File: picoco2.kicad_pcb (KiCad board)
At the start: 2 copper layers, 54.5 x 103.4 mm, 41 parts, among them J1 Conn_01x03_Female, J2 Micro_SD_Card, J3 Conn_01x03_Female, Q1 Q_NMOS_GDS, SW1 SW_Push, SW2 SW_Push, U1 PicoW, U2 scd30, U3 ssd1306, U4 PCF8523T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

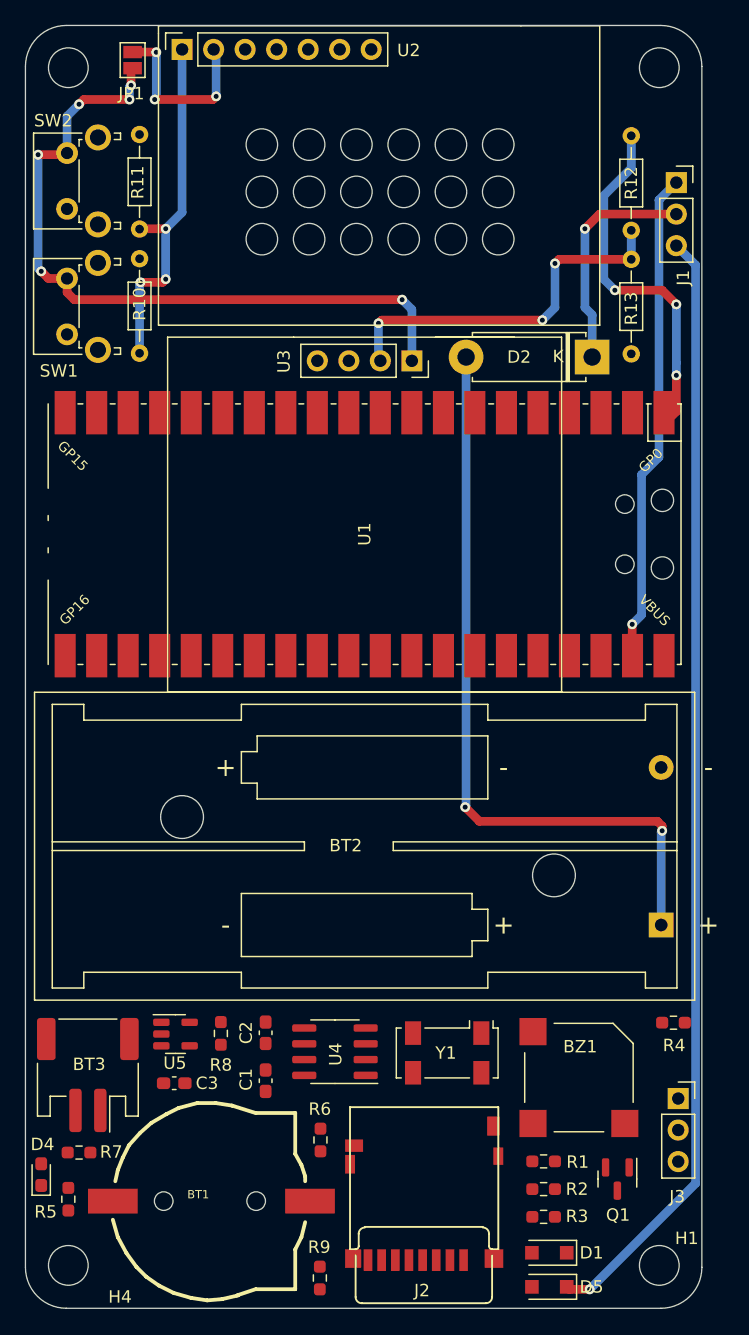
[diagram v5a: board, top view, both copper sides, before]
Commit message: finished positioning of holes and parts
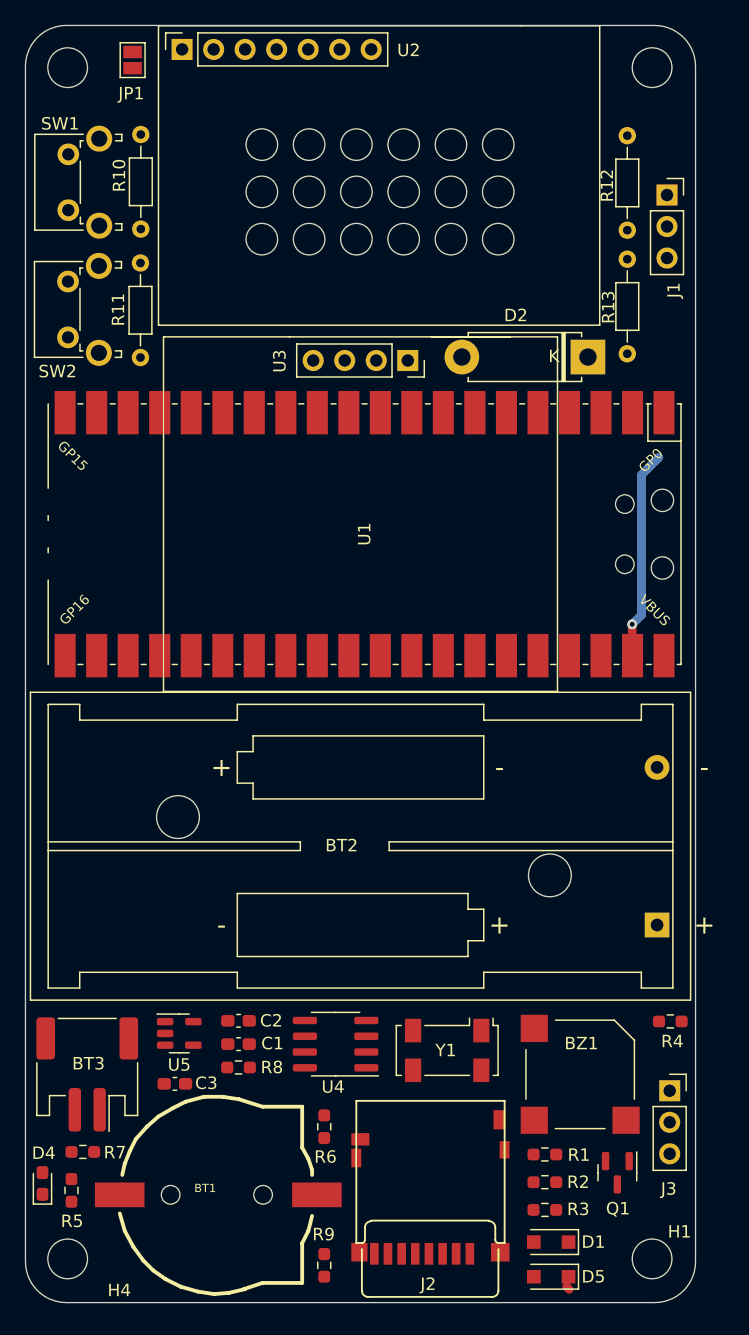
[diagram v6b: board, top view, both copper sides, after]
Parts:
- moved SW2 10.4 mm to (3.43, 25.1)
- moved R11 10.4 mm to (9.27, 26.8)
- moved R10 10.0 mm to (9.30, 16.4)
- moved SW1 10.0 mm to (3.45, 14.9)
- moved C1 3.67 mm to (17.2, 82.1), turned to 180 degrees
- moved R8 3.09 mm to (17.2, 84.0), turned to 0 degrees
- moved C2 2.39 mm to (17.2, 80.2), turned to 180 degrees
- moved J1 1.25 mm to (51.7, 13.7)
- moved R6 1.11 mm to (24.1, 88.7)
- moved R9 1.08 mm to (24.1, 99.9)
- moved J3 0.93 mm to (51.9, 85.9)
- moved D1 0.88 mm to (42.4, 98.0)
- moved D5 0.83 mm to (42.4, 100.8)
- moved H1 0.78 mm to (50.5, 99.4)
- moved R5 0.76 mm to (3.71, 93.9)
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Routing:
- net Net-(D5-Pad1): track 90.2 -> 0.29 mm, vias 1 -> 0
- net VBAT_AAA: track 60.8 -> 0.00 mm, vias 2 -> 0
- net +3V3: track 59.1 -> 0.22 mm, vias 6 -> 0
- net GND: track 59.0 -> 0.18 mm, vias 6 -> 0
- net SDA: track 29.2 -> 0.00 mm, vias 3 -> 0
- net VSYS: track 38.7 -> 16.0 mm
- net Net-(D1-Pad1): track 18.4 -> 0.00 mm, vias 1 -> 0
- net SCD30_GND: track 14.7 -> 0.29 mm, vias 3 -> 0
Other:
- board size 54.5 x 103.4 mm -> 54 x 102.9 mm

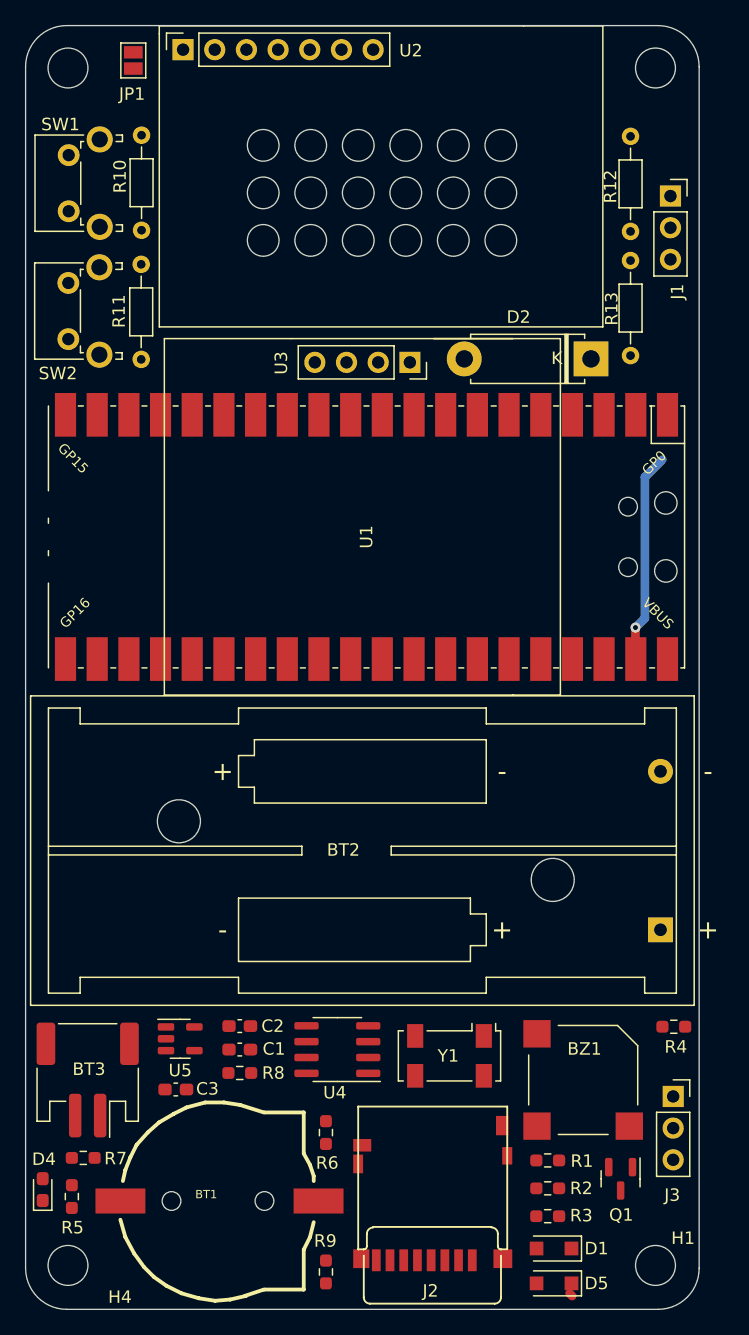
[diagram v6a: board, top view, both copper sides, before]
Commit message: routed power lines
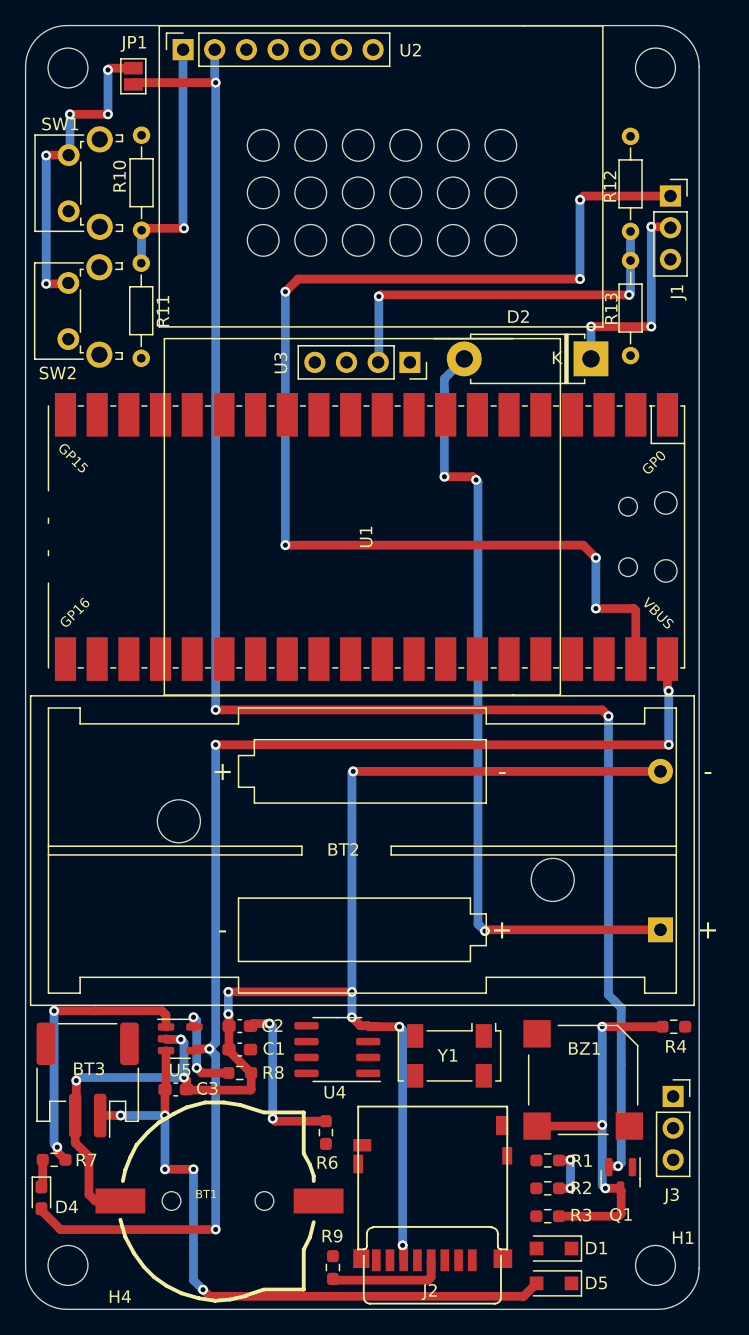
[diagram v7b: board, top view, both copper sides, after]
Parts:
- removed R5: R, Resistor_SMD:R_0603_1608Metric_Pad0.98x0.95mm_HandSolder
- moved R11 7.71 mm to (9.27, 19.1), turned to -90 degrees
- moved R7 2.34 mm to (2.29, 90.9)
- moved JP1 1.27 mm to (8.64, 4.06), turned to -90 degrees
- moved D4 0.67 mm to (1.27, 94.0), turned to -90 degrees
- moved R9 0.66 mm to (24.6, 99.6)
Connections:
- D5 pad 1: Net-(D5-Pad1) -> Net-(D1-Pad1)
- J1 pad 3: Net-(D5-Pad1) -> unconnected-(J1-Pad3)
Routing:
- net GND: track 0.18 -> 174.9 mm, vias 0 -> 18
- net SCD30_GND: track 0.29 -> 129.0 mm, vias 0 -> 4
- net VBUS: track 0.00 -> 99.4 mm, vias 0 -> 5
- net +3V3: track 0.22 -> 78.4 mm, vias 0 -> 7
- net VSYS: track 16.0 -> 93.8 mm, vias 1 -> 6
- net VBAT_AAA: track 0.00 -> 63.3 mm, vias 0 -> 3
- net VBAT_LIPO: track 0.00 -> 54.9 mm, vias 0 -> 5
- net Net-(R7-Pad2): track 0.00 -> 22.4 mm, vias 0 -> 2
- net Net-(D1-Pad1): track 0.00 -> 17.0 mm, vias 0 -> 3
- net Net-(R8-Pad1): track 0.00 -> 7.69 mm, vias 0 -> 2
- net Net-(D4-Pad1): track 0.00 -> 2.22 mm

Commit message: finally finished routing power
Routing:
- net +3V3: track 78.4 -> 118.3 mm, vias 7 -> 11
- net VBAT_AAA: track 63.3 -> 90.3 mm, vias 3 -> 5
- net GND: track 174.9 -> 188.3 mm, vias 18 -> 19
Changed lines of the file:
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@@
     (style (thickness 0.15) (arrow_length 1.27) (text_position_mode 0) (extension_height 0.58642) (extension_offset 0.5) keep_text_aligned)
   )
+  (segment (start 42.7717 93.218) (end 45.280967 93.218) (width 0.7) (layer "F.Cu") (net 31))
   (segment (start 32.258 100.584) (end 24.7415 100.584) (width 0.7) (layer "F.Cu") (net 31))
   (segment (start 20.0171 87.8351) (end 19.812 87.63) (width 0.7) (layer "F.Cu") (net 31))
+  (segment (start 32.766 92.202) (end 32.9602 92.0078) (width 0.7) (layer "F.Cu") (net 31))
+  (segment (start 45.280967 93.218) (end 45.327225 93.264258) (width 0.7) (layer "F.Cu") (net 31))
   (segment (start 19.558 80.01) (end 18.2361 80.01) (width 0.7) (layer "F.Cu") (net 31))
   (segment (start 48.387 21.59) (end 28.448 21.59) (width 0.7) (layer "F.Cu") (net 31))
-  (segment (start 43.688 93.218) (end 42.7717 93.218) (width 0.7) (layer "F.Cu") (net 31))
   (segment (start 24.7415 100.584) (end 24.638 100.4805) (width 0.7) (layer "F.Cu") (net 31))
   (segment (start 18.2361 80.01) (end 18.0329 80.2132) (width 0.7) (layer "F.Cu") (net 31))
   (segment (start 28.448 21.59) (end 28.321 21.717) (width 0.7) (layer "F.Cu") (net 31))
+  (segment (start 45.466 96.774) (end 32.512 96.774) (width 0.7) (layer "F.Cu") (net 31))
+  (segment (start 32.512 97.536) (end 32.512 96.774) (width 0.7) (layer "F.Cu") (net 31))
+  (segment (start 32.5136 97.5376) (end 32.512 97.536) (width 0.7) (layer "F.Cu") (net 31))
   (segment (start 24.0792 87.8351) (end 20.0171 87.8351) (width 0.7) (layer "F.Cu") (net 31))
+  (segment (start 24.0792 87.8351) (end 32.4631 87.8351) (width 0.7) (layer "F.Cu") (net 31))
+  (segment (start 45.2785 90.932) (end 42.8225 90.932) (width 0.7) (layer "F.Cu") (net 31))
+  (segment (start 32.5136 98.988) (end 32.5136 97.5376) (width 0.7) (layer "F.Cu") (net 31))
   (segment (start 32.5136 98.988) (end 32.5136 100.3284) (width 0.7) (layer "F.Cu") (net 31))
   (segment (start 12.7 16.256) (end 9.4488 16.256) (width 0.7) (layer "F.Cu") (net 31))
   (segment (start 32.5136 100.3284) (end 32.258 100.584) (width 0.7) (layer "F.Cu") (net 31))
-  (segment (start 43.6372 90.9828) (end 43.688 90.932) (width 0.7) (layer "F.Cu") (net 31))
-  (segment (start 42.7717 90.9828) (end 43.6372 90.9828) (width 0.7) (layer "F.Cu") (net 31))
+  (segment (start 42.8225 90.932) (end 42.7717 90.9828) (width 0.7) (layer "F.Cu") (net 31))
+  (segment (start 32.4631 87.8351) (end 32.512 87.884) (width 0.7) (layer "F.Cu") (net 31))
   (segment (start 9.4488 16.256) (end 9.2964 16.4084) (width 0.7) (layer "F.Cu") (net 31))
-  (via (at 43.688 93.218) (size 0.8) (drill 0.4) (layers "F.Cu" "B.Cu") (net 31))
+  (via (at 45.327225 93.264258) (size 0.8) (drill 0.4) (layers "F.Cu" "B.Cu") (net 31))
   (via (at 28.321 21.717) (size 0.8) (drill 0.4) (layers "F.Cu" "B.Cu") (net 31))
   (via (at 12.7 16.256) (size 0.8) (drill 0.4) (layers "F.Cu" "B.Cu") (net 31))
+  (via (at 32.512 96.774) (size 0.8) (drill 0.4) (layers "F.Cu" "B.Cu") (net 31))
+  (via (at 45.2785 90.932) (size 0.8) (drill 0.4) (layers "F.Cu" "B.Cu") (net 31))
   (via (at 19.812 87.63) (size 0.8) (drill 0.4) (layers "F.Cu" "B.Cu") (net 31))
+  (via (at 32.766 92.202) (size 0.8) (drill 0.4) (layers "F.Cu" "B.Cu") (net 31))
+  (via (at 45.466 96.774) (size 0.8) (drill 0.4) (layers "F.Cu" "B.Cu") (net 31))
   (via (at 19.558 80.01) (size 0.8) (drill 0.4) (layers "F.Cu" "B.Cu") (net 31))
+  (via (at 32.512 87.884) (size 0.8) (drill 0.4) (layers "F.Cu" "B.Cu") (net 31))
   (via (at 48.387 21.59) (size 0.8) (drill 0.4) (layers "F.Cu" "B.Cu") (net 31))
-  (via (at 43.688 90.932) (size 0.8) (drill 0.4) (layers "F.Cu" "B.Cu") (net 31))
+  (segment (start 32.512 87.884) (end 32.512 91.948) (width 0.7) (layer "B.Cu") (net 31))
   (segment (start 48.5 18.8368) (end 48.5 16.5) (width 0.7) (layer "B.Cu") (net 31))
   (segment (start 12.6238 16.1798) (end 12.7 16.256) (width 0.7) (layer "B.Cu") (net 31))
+  (segment (start 32.512 96.774) (end 32.512 92.456) (width 0.7) (layer "B.Cu") (net 31))
   (segment (start 48.5 18.8368) (end 48.5 21.477) (width 0.7) (layer "B.Cu") (net 31))
   (segment (start 19.812 87.63) (end 19.812 80.264) (width 0.7) (layer "B.Cu") (net 31))
   (segment (start 28.448 26.8732) (end 28.6004 27.0256) (width 0.7) (layer "B.Cu") (net 31))
+  (segment (start 45.327225 90.980725) (end 45.2785 90.932) (width 0.7) (layer "B.Cu") (net 31))
   (segment (start 9.2964 16.4084) (end 9.2964 19.0246) (width 0.7) (layer "B.Cu") (net 31))
+  (segment (start 45.327225 93.264258) (end 45.327225 96.635225) (width 0.7) (layer "B.Cu") (net 31))
+  (segment (start 45.327225 96.635225) (end 45.466 96.774) (width 0.7) (layer "B.Cu") (net 31))
   (segment (start 12.6238 1.9304) (end 12.6238 16.1798) (width 0.7) (layer "B.Cu") (net 31))
-  (segment (start 43.688 90.932) (end 43.688 93.218) (width 0.7) (layer "B.Cu") (net 31))
   (segment (start 19.812 80.264) (end 19.558 80.01) (width 0.7) (layer "B.Cu") (net 31))
+  (segment (start 45.327225 93.264258) (end 45.327225 90.980725) (width 0.7) (layer "B.Cu") (net 31))
   (segment (start 28.321 26.949) (end 28.27 27) (width 0.7) (layer "B.Cu") (net 31))
+  (segment (start 32.512 92.456) (end 32.766 92.202) (width 0.7) (layer "B.Cu") (net 31))
   (segment (start 9.2964 19.0246) (end 9.271 19.05) (width 0.7) (layer "B.Cu") (net 31))
   (segment (start 28.321 21.717) (end 28.321 26.949) (width 0.7) (layer "B.Cu") (net 31))
+  (segment (start 32.512 91.948) (end 32.766 92.202) (width 0.7) (layer "B.Cu") (net 31))
   (segment (start 48.5 21.477) (end 48.387 21.59) (width 0.7) (layer "B.Cu") (net 31))
   (segment (start 50.9016 59.7916) (end 26.2636 59.7916) (width 0.7) (layer "F.Cu") (net 32))
@@
   (segment (start 6.746 3.414) (end 6.604 3.556) (width 0.7) (layer "F.Cu") (net 32))
   (segment (start 1.651 20.701) (end 3.3605 20.701) (width 0.7) (layer "F.Cu") (net 32))
+  (segment (start 42.3582 94.4282) (end 30.2858 94.4282) (width 0.7) (layer "F.Cu") (net 32))
   (segment (start 5.08 93.726) (end 5.5888 94.2348) (width 0.7) (layer "F.Cu") (net 32))
   (segment (start 27.4686 80.1878) (end 26.8478 80.1878) (width 0.7) (layer "F.Cu") (net 32))
@@
   (segment (start 42.7717 95.4532) (end 47.5488 95.4532) (width 0.7) (layer "F.Cu") (net 32))
   (segment (start 27.5448 80.264) (end 27.4686 80.1878) (width 0.7) (layer "F.Cu") (net 32))
+  (segment (start 42.7717 95.4532) (end 42.7717 94.8417) (width 0.7) (layer "F.Cu") (net 32))
   (segment (start 12.9021 84.5301) (end 12.7 84.328) (width 0.7) (layer "F.Cu") (net 32))
+  (segment (start 30.2858 94.4282) (end 30.226 94.488) (width 0.7) (layer "F.Cu") (net 32))
+  (segment (start 42.7717 94.8417) (end 42.3582 94.4282) (width 0.7) (layer "F.Cu") (net 32))
   (segment (start 16.3079 82.0928) (end 16.3079 82.1974) (width 0.7) (layer "F.Cu") (net 32))
   (segment (start 16.3079 82.1974) (end 18.0829 83.9724) (width 0.7) (layer "F.Cu") (net 32))
@@
   (via (at 6.604 7.112) (size 0.8) (drill 0.4) (layers "F.Cu" "B.Cu") (net 32))
   (via (at 1.651 10.414) (size 0.8) (drill 0.4) (layers "F.Cu" "B.Cu") (net 32))
+  (via (at 30.226 94.488) (size 0.8) (drill 0.4) (layers "F.Cu" "B.Cu") (net 32))
   (via (at 46.482 93.218) (size 0.8) (drill 0.4) (layers "F.Cu" "B.Cu") (net 32))
   (via (at 26.162 79.502) (size 0.8) (drill 0.4) (layers "F.Cu" "B.Cu") (net 32))
@@
   (segment (start 20.828 21.336) (end 20.828 41.656) (width 0.7) (layer "B.Cu") (net 47))
   (segment (start 45.72 42.672) (end 45.72 46.736) (width 0.7) (layer "B.Cu") (net 47))
+  (segment (start 36.9316 72.4916) (end 39.5224 72.4916) (width 0.7) (layer "F.Cu") (net 53))
   (segment (start 36.83 72.5932) (end 36.9316 72.4916) (width 0.7) (layer "F.Cu") (net 53))
   (segment (start 35.8648 36.1696) (end 36.1188 36.4236) (width 0.7) (layer "F.Cu") (net 53))
   (segment (start 33.5788 36.1696) (end 35.8648 36.1696) (width 0.7) (layer "F.Cu") (net 53))
-  (segment (start 36.9316 72.4916) (end 50.9016 72.4916) (width 0.7) (layer "F.Cu") (net 53))
+  (segment (start 39.5224 72.4916) (end 50.9016 72.4916) (width 0.7) (layer "F.Cu") (net 53))
+  (segment (start 40.9672 98.044) (end 39.624 98.044) (width 0.7) (layer "F.Cu") (net 53))
+  (via (at 39.624 98.044) (size 0.8) (drill 0.4) (layers "F.Cu" "B.Cu") (net 53))
   (via (at 36.83 72.5932) (size 0.8) (drill 0.4) (layers "F.Cu" "B.Cu") (net 53))
   (via (at 36.1188 36.4236) (size 0.8) (drill 0.4) (layers "F.Cu" "B.Cu") (net 53))
   (via (at 33.5788 36.1696) (size 0.8) (drill 0.4) (layers "F.Cu" "B.Cu") (net 53))
+  (via (at 39.5224 72.4916) (size 0.8) (drill 0.4) (layers "F.Cu" "B.Cu") (net 53))
   (segment (start 33.5788 29.21) (end 33.5788 36.1696) (width 0.7) (layer "B.Cu") (net 53))
   (segment (start 36.2712 72.0344) (end 36.83 72.5932) (width 0.7) (layer "B.Cu") (net 53))
   (segment (start 35.17 26.7208) (end 33.5788 28.312) (width 0.7) (layer "B.Cu") (net 53))
   (segment (start 36.2712 36.576) (end 36.2712 49.7332) (width 0.7) (layer "B.Cu") (net 53))
+  (segment (start 39.624 98.044) (end 39.624 72.5932) (width 0.7) (layer "B.Cu") (net 53))
   (segment (start 36.2712 49.7332) (end 36.2712 72.0344) (width 0.7) (layer "B.Cu") (net 53))
   (segment (start 33.5788 28.312) (end 33.5788 29.21) (width 0.7) (layer "B.Cu") (net 53))
+  (segment (start 39.624 72.5932) (end 39.5224 72.4916) (width 0.7) (layer "B.Cu") (net 53))
   (segment (start 36.1188 36.4236) (end 36.2712 36.576) (width 0.7) (layer "B.Cu") (net 53))
   (segment (start 7.62 87.376) (end 5.9836 87.376) (width 0.7) (layer "F.Cu") (net 54))
